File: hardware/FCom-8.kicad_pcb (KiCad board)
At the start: 2 copper layers, 94 x 127 mm, 86 parts, among them J101 Conn_01x04, J201 4090 USB-C, J202 9V battery, SW101 SW_DIP_x08, SW102 SW_DIP_x08, SW104 SW_DIP_x04, SW105 G19AP, SW301 Q/1/STOP, SW302 W/2/CH0, SW303 E/3/CH1, SW304 R/4/CH2, SW305 T/5/CH3, SW306 Y/6/_, SW307 U/7/-, SW308 I/8/+, SW309 O/9/=, SW310 P/0, SW311 A/!/`, SW312 S/"/CH4, SW313 D/$/CH5, SW314 F/%/CH6, SW315 G/^/CH7, SW316 H/&/{, SW317 J/*/}, SW318 K/(/[, SW319 L/)/], SW320 BKSP/DEL, SW321 SHIFT, SW322 Z/\/|, SW323 X/;/:, SW324 C/'/@, SW325 V/#/~, SW326 B/,/<, SW327 N/./>, SW328 M///?, SW329 SYM, SW330 SPC/ENT, U101 W65C02S6TPG-14, U102 AS6C1008-55PCN, U103 W65C22N6TPG-14, U104 74LS04, U105 74LS08, U106 74LS21, U201 LM1117T-5.0, U301 MCP23S17_SP, U302 NHD-0420DZ-FL-YBW, Y101 ECS-100AX-010

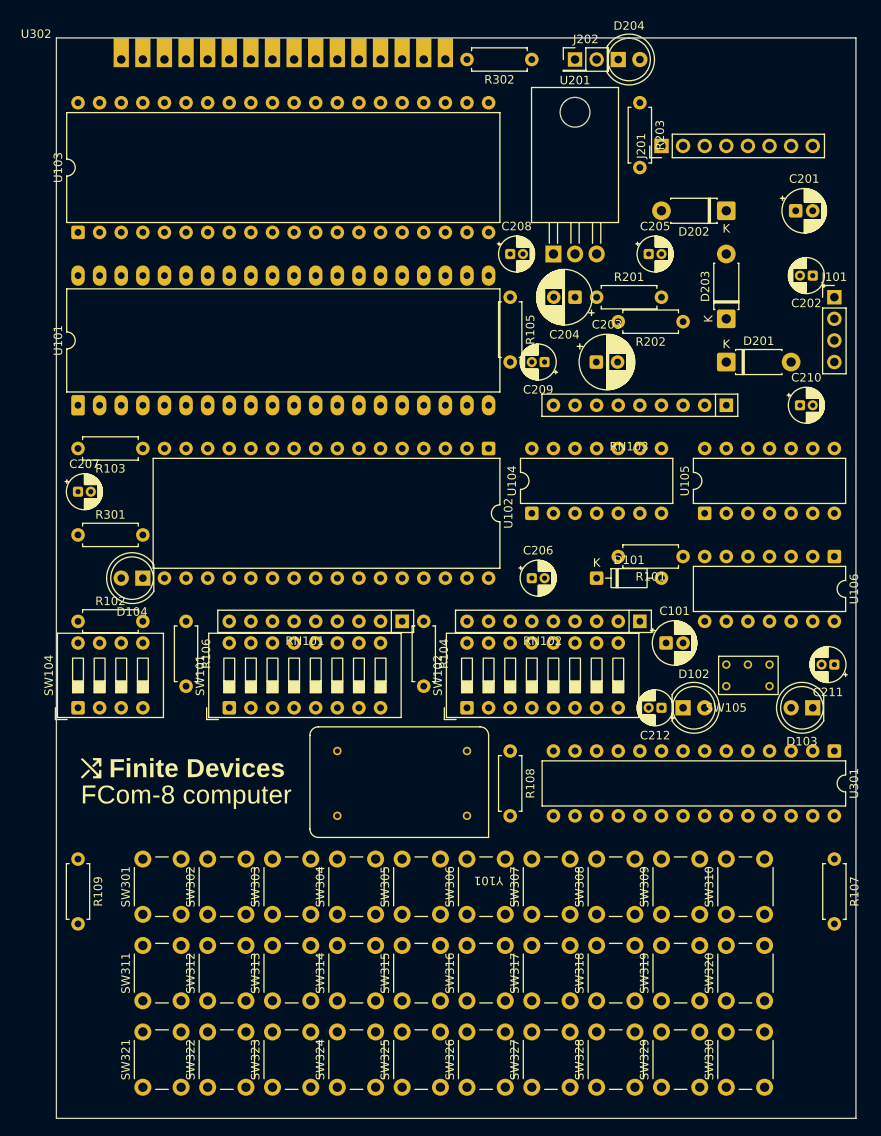
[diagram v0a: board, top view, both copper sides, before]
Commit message: Finish rough component wiring layout
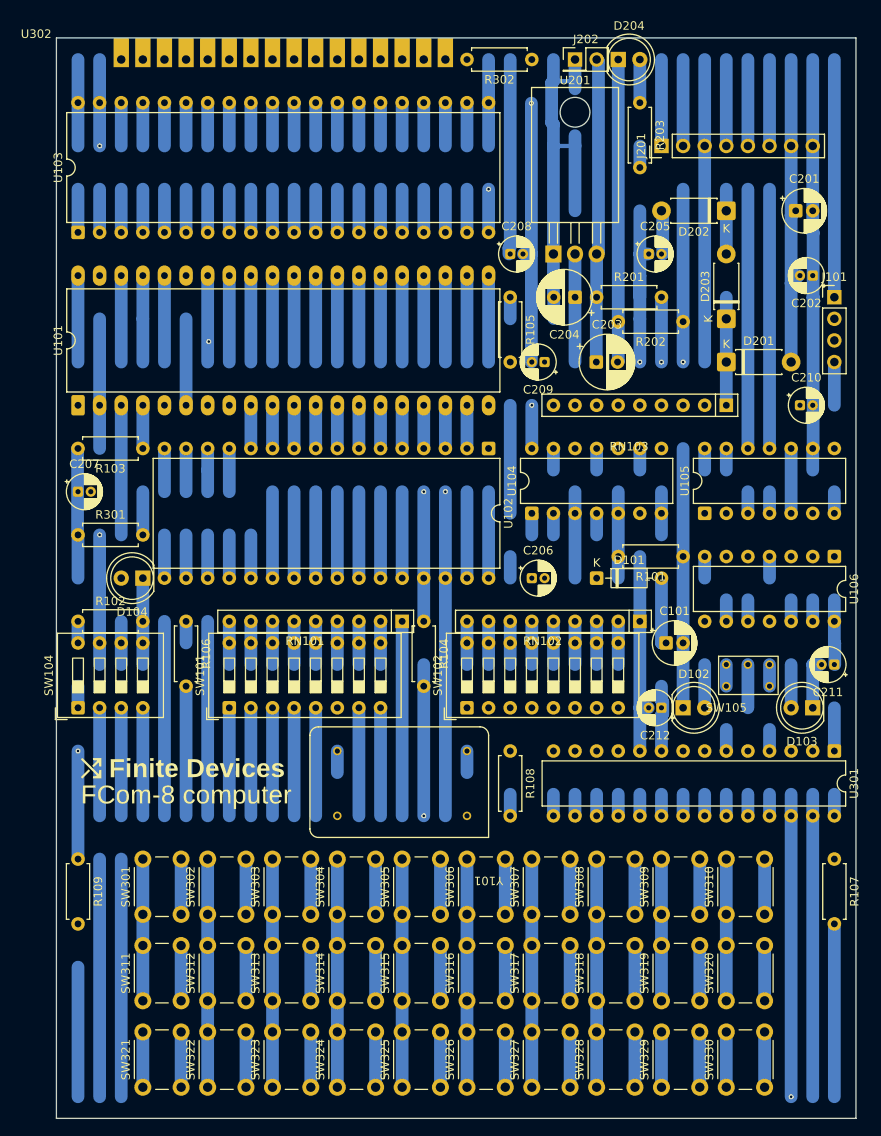
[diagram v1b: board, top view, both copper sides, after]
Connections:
- SW104 pad 3: GND -> KB_SWA
- SW104 pad 4: GND -> KB_SWB
- SW104 pad 5: KB_SWB -> GND
- SW104 pad 6: KB_SWA -> GND
- U103 pad 34: ~{RESET} -> VCC
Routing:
- net GND: track 0.00 -> 831.3 mm, vias 0 -> 3
- net VCC: track 0.00 -> 527.6 mm, vias 0 -> 2
- net VBS: track 0.00 -> 190.5 mm
- net Net-(U301-GPB5): track 0.00 -> 180.5 mm
- net +5V: track 0.00 -> 173.7 mm
- net Net-(U301-GPB6): track 0.00 -> 169.4 mm
- net KB_INT: track 0.00 -> 153.2 mm
- net Net-(U301-GPB7): track 0.00 -> 149.9 mm
- net ~{RAM_CS}: track 0.00 -> 149.0 mm
- net /A12: track 0.00 -> 145.5 mm
- net PHI2O: track 0.00 -> 135.9 mm, vias 0 -> 1
- net /D7: track 0.00 -> 134.7 mm
- net /D4: track 0.00 -> 134.1 mm
- net /D3: track 0.00 -> 134.1 mm
- net /D6: track 0.00 -> 133.8 mm
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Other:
- copper layers 2 -> 12
